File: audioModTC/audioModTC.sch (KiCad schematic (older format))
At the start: 41 parts, among them J1 Screw_Terminal_01x02, J2 703W-00/52, Q1 IRFP360LCPBF, Q2 IRFP360LCPBF, U1 NCP1117-12V, U2 74HC14, U3 NCP1117-5V, U4 UCC37321P, U5 UCC37322P

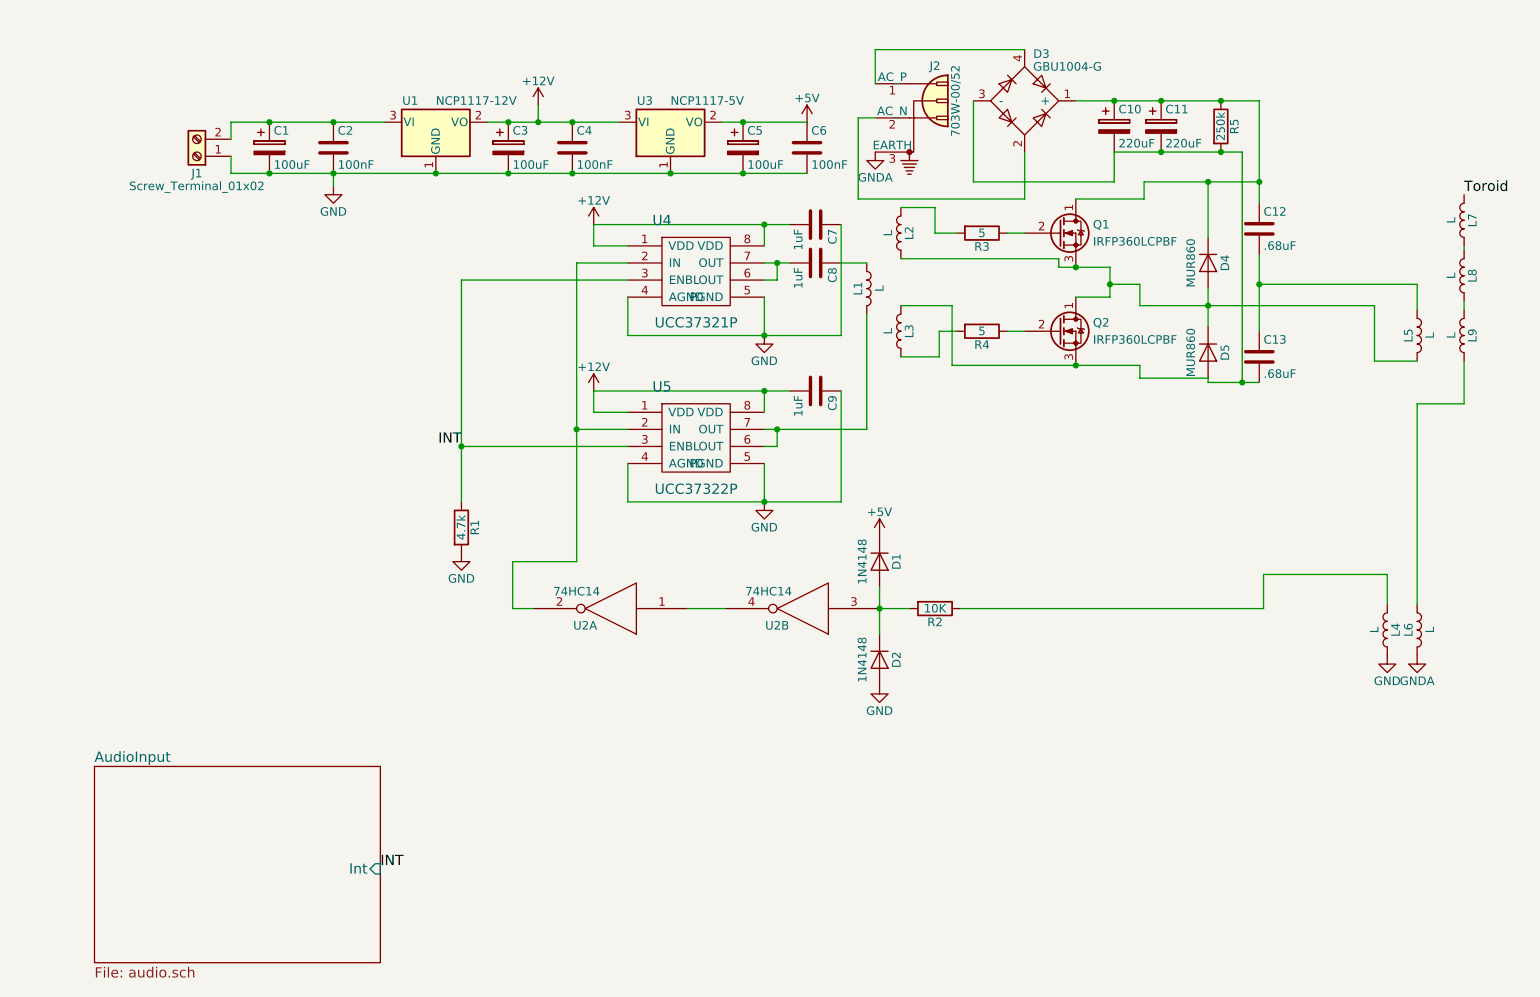
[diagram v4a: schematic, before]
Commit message: Finished footprints
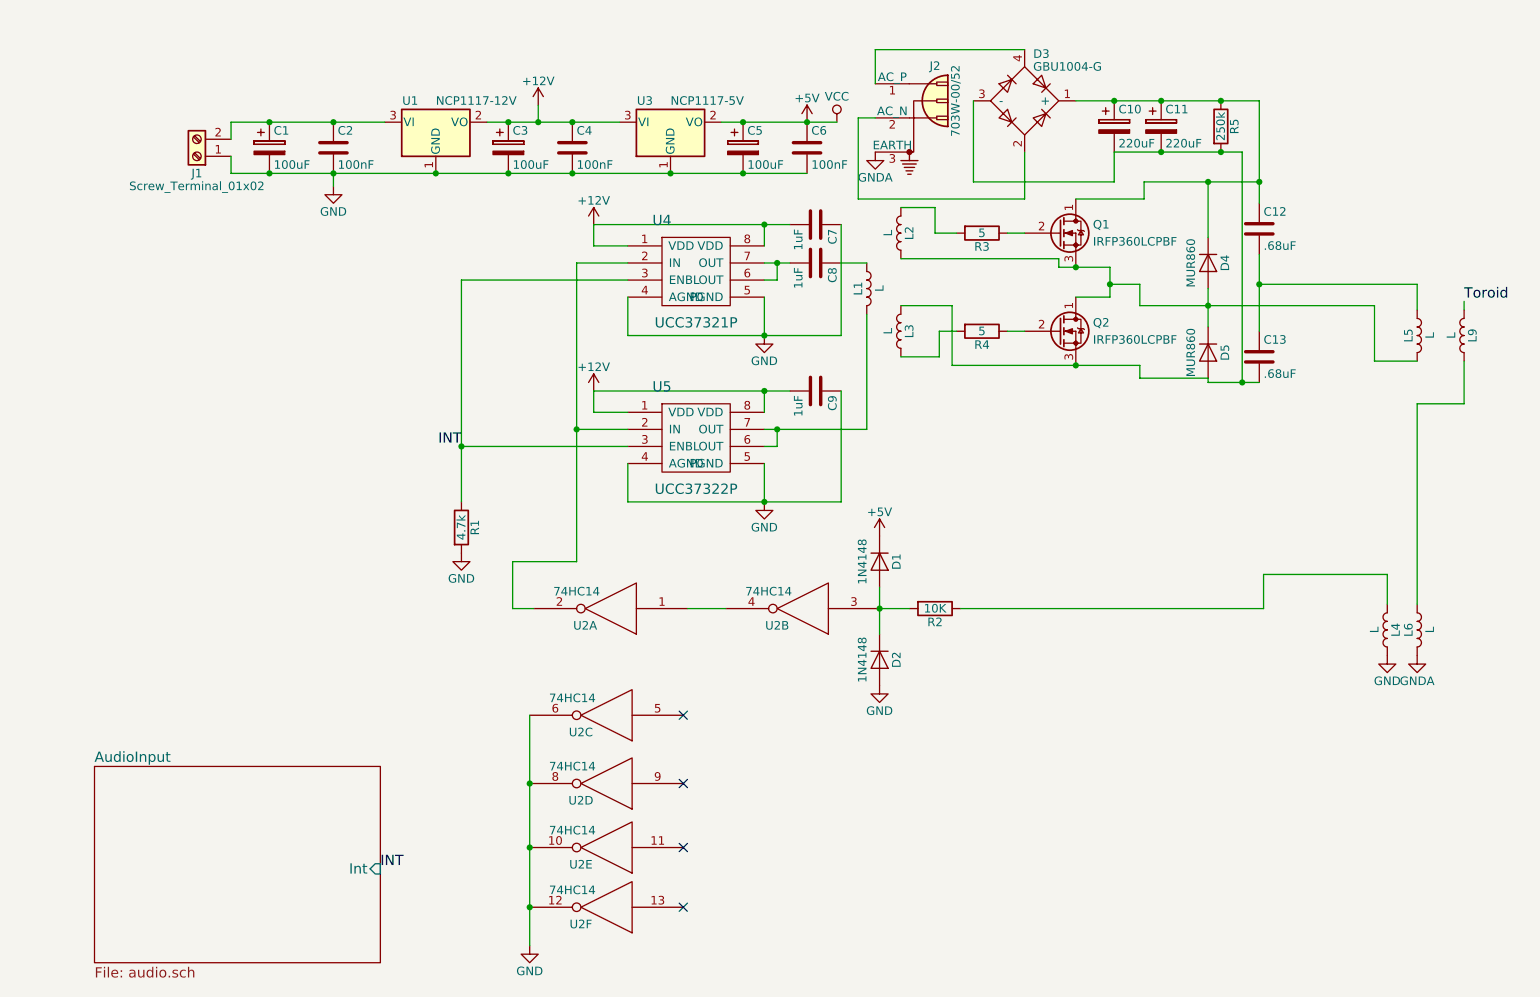
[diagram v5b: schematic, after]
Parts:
- removed L7, L8: L, symbol L
- added unit 3 of U2
- added unit 4 of U2
- added unit 5 of U2
- added unit 6 of U2
- L1, L2, L3, L4, L5, L6, L9: footprint (none) -> Inductors_THT:L_Radial_D7.0mm_P3.00mm
- U2: footprint (none) -> Housings_DIP:DIP-14_W7.62mm
- U4, U5: footprint (none) -> Housings_DIP:DIP-8_W7.62mm
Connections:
- net VCC is gone; now on net +5V: U2.14 (VCC), U2.14 (VCC)
- net +5V: now also U2.14 (VCC), U2.14 (VCC), U2.14 (VCC), U2.14 (VCC)
- net GND: now also U2.10, U2.12, U2.6, U2.7 (GND), U2.7 (GND), U2.7 (GND), U2.7 (GND), U2.8
- net Toroid: now also L9.2
- no-connect marks 0 -> 4
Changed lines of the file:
@@
 Connection ~ 3875 1625
 Wire Wire Line
-	5125 1325 5625 1325
+	5125 1325 5800 1325
 Connection ~ 5250 1325
 Connection ~ 4825 1625
@@
 F 0 "L5" V 9150 2575 50  0000 C CNN
 F 1 "L" V 9275 2575 50  0000 C CNN
-F 2 "" H 9200 2575 50  0001 C CNN
+F 2 "Inductors_THT:L_Radial_D7.0mm_P3.00mm" H 9200 2575 50  0001 C CNN
 F 3 "" H 9200 2575 50  0001 C CNN
 	1    9200 2575
@@
 F 0 "L3" V 6125 2550 50  0000 C CNN
 F 1 "L" V 6250 2550 50  0000 C CNN
-F 2 "" H 6175 2550 50  0001 C CNN
+F 2 "Inductors_THT:L_Radial_D7.0mm_P3.00mm" H 6175 2550 50  0001 C CNN
 F 3 "" H 6175 2550 50  0001 C CNN
 	1    6175 2550
@@
 F 0 "L2" V 6125 1975 50  0000 C CNN
 F 1 "L" V 6250 1975 50  0000 C CNN
-F 2 "" H 6175 1975 50  0001 C CNN
+F 2 "Inductors_THT:L_Radial_D7.0mm_P3.00mm" H 6175 1975 50  0001 C CNN
 F 3 "" H 6175 1975 50  0001 C CNN
 	1    6175 1975
@@
 F 0 "L1" V 5925 2300 50  0000 C CNN
 F 1 "L" V 6050 2300 50  0000 C CNN
-F 2 "" H 5975 2300 50  0001 C CNN
+F 2 "Inductors_THT:L_Radial_D7.0mm_P3.00mm" H 5975 2300 50  0001 C CNN
 F 3 "" H 5975 2300 50  0001 C CNN
 	1    5975 2300
@@
 F 0 "U4" H 4775 2500 60  0000 C CNN
 F 1 "UCC37321P" H 4975 1900 60  0000 C CNN
-F 2 "" H 4925 2200 60  0001 C CNN
+F 2 "Housings_DIP:DIP-8_W7.62mm" H 4925 2200 60  0001 C CNN
 F 3 "" H 4925 2200 60  0001 C CNN
 	1    4975 2200
@@
 F 0 "U5" H 4775 3475 60  0000 C CNN
 F 1 "UCC37322P" H 4975 2875 60  0000 C CNN
-F 2 "" H 4925 3175 60  0001 C CNN
+F 2 "Housings_DIP:DIP-8_W7.62mm" H 4925 3175 60  0001 C CNN
 F 3 "" H 4925 3175 60  0001 C CNN
 	1    4975 3175
@@
 F 0 "U2" H 4625 4275 50  0000 C CNN
 F 1 "74HC14" H 4675 4075 50  0000 C CNN
-F 2 "" H 4475 4175 50  0001 C CNN
+F 2 "Housings_DIP:DIP-14_W7.62mm" H 4475 4175 50  0001 C CNN
 F 3 "" H 4475 4175 50  0001 C CNN
 	1    4475 4175
@@
 F 0 "U2" H 5750 4275 50  0000 C CNN
 F 1 "74HC14" H 5800 4075 50  0000 C CNN
-F 2 "" H 5600 4175 50  0001 C CNN
+F 2 "Housings_DIP:DIP-14_W7.62mm" H 5600 4175 50  0001 C CNN
 F 3 "" H 5600 4175 50  0001 C CNN
 	2    5600 4175
@@
 F 0 "L6" V 9150 4300 50  0000 C CNN
 F 1 "L" V 9275 4300 50  0000 C CNN
-F 2 "" H 9200 4300 50  0001 C CNN
+F 2 "Inductors_THT:L_Radial_D7.0mm_P3.00mm" H 9200 4300 50  0001 C CNN
 F 3 "" H 9200 4300 50  0001 C CNN
 	1    9200 4300
@@
 F 0 "L4" V 8975 4300 50  0000 C CNN
 F 1 "L" V 9100 4300 50  0000 C CNN
-F 2 "" H 9025 4300 50  0001 C CNN
+F 2 "Inductors_THT:L_Radial_D7.0mm_P3.00mm" H 9025 4300 50  0001 C CNN
 F 3 "" H 9025 4300 50  0001 C CNN
 	1    9025 4300
@@
 F 0 "L9" V 9425 2575 50  0000 C CNN
 F 1 "L" V 9550 2575 50  0000 C CNN
-F 2 "" H 9475 2575 50  0001 C CNN
+F 2 "Inductors_THT:L_Radial_D7.0mm_P3.00mm" H 9475 2575 50  0001 C CNN
 F 3 "" H 9475 2575 50  0001 C CNN
 	1    9475 2575
 	-1   0    0    1
 $EndComp
-$Comp
-L L L8
-U 1 1 5A4AC75A
-P 9475 2225
-F 0 "L8" V 9425 2225 50  0000 C CNN
-F 1 "L" V 9550 2225 50  0000 C CNN
-F 2 "" H 9475 2225 50  0001 C CNN
-F 3 "" H 9475 2225 50  0001 C CNN
-	1    9475 2225
-	-1   0    0    1
-$EndComp
-$Comp
-L L L7
-U 1 1 5A4AC7D1
-P 9475 1900
-F 0 "L7" V 9425 1900 50  0000 C CNN
-F 1 "L" V 9550 1900 50  0000 C CNN
-F 2 "" H 9475 1900 50  0001 C CNN
-F 3 "" H 9475 1900 50  0001 C CNN
-	1    9475 1900
-	-1   0    0    1
-$EndComp
 Wire Wire Line
 	9200 4150 9200 2975
@@
 	9475 2975 9475 2725
 Wire Wire Line
-	9475 2050 9475 2075
-Wire Wire Line
 	9475 2375 9475 2425
-Text Label 9475 1750 0    60   ~ 0
+Text Label 9475 2375 0    60   ~ 0
 Toroid
 $Sheet
@@
 Wire Wire Line
 	5925 1300 6025 1300
+$Comp
+L 74HC14 U2
+U 3 1 5A4E733A
+P 4450 4800
+F 0 "U2" H 4600 4900 50  0000 C CNN
+F 1 "74HC14" H 4650 4700 50  0000 C CNN
+F 2 "Housings_DIP:DIP-14_W7.62mm" H 4450 4800 50  0001 C CNN
+F 3 "" H 4450 4800 50  0001 C CNN
+	3    4450 4800
+	-1   0    0    1
+$EndComp
+$Comp
+L 74HC14 U2
+U 4 1 5A4E744D
+P 4450 5200
+F 0 "U2" H 4600 5300 50  0000 C CNN
+F 1 "74HC14" H 4650 5100 50  0000 C CNN
+F 2 "Housings_DIP:DIP-14_W7.62mm" H 4450 5200 50  0001 C CNN
+F 3 "" H 4450 5200 50  0001 C CNN
+	4    4450 5200
+	-1   0    0    1
+$EndComp
+$Comp
+L 74HC14 U2
+U 5 1 5A4E7818
+P 4450 5575
+F 0 "U2" H 4600 5675 50  0000 C CNN
+F 1 "74HC14" H 4650 5475 50  0000 C CNN
+F 2 "Housings_DIP:DIP-14_W7.62mm" H 4450 5575 50  0001 C CNN
+F 3 "" H 4450 5575 50  0001 C CNN
+	5    4450 5575
+	-1   0    0    1
+$EndComp
+$Comp
+L 74HC14 U2
+U 6 1 5A4E7919
+P 4450 5925
+F 0 "U2" H 4600 6025 50  0000 C CNN
+F 1 "74HC14" H 4650 5825 50  0000 C CNN
+F 2 "Housings_DIP:DIP-14_W7.62mm" H 4450 5925 50  0001 C CNN
+F 3 "" H 4450 5925 50  0001 C CNN
+	6    4450 5925
+	-1   0    0    1
+$EndComp
+NoConn ~ 4900 4800
+NoConn ~ 4900 5200
+NoConn ~ 4900 5575
+NoConn ~ 4900 5925
+$Comp
+L GND #PWR014
+U 1 1 5A4E85FF
+P 4000 6150
+F 0 "#PWR014" H 4000 5900 50  0001 C CNN
+F 1 "GND" H 4000 6000 50  0000 C CNN
+F 2 "" H 4000 6150 50  0001 C CNN
+F 3 "" H 4000 6150 50  0001 C CNN
+	1    4000 6150
+	1    0    0    -1
+$EndComp
+Wire Wire Line
+	4000 4800 4000 6150
+Connection ~ 4000 5200
+Connection ~ 4000 5575
+Connection ~ 4000 5925
+$Comp
+L VCC #PWR015
+U 1 1 5A4F18EE
+P 5800 1325
+F 0 "#PWR015" H 5800 1175 50  0001 C CNN
+F 1 "VCC" H 5800 1475 50  0000 C CNN
+F 2 "" H 5800 1325 50  0001 C CNN
+F 3 "" H 5800 1325 50  0001 C CNN
+	1    5800 1325
+	1    0    0    -1
+$EndComp
+Connection ~ 5625 1325
 $EndSCHEMATC

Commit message: Finished footprints fo real
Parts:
- removed L1, L2, L3, L4, L6: L, Inductors_THT:L_Radial_D7.0mm_P3.00mm, symbol L
- added T1: Transformer_1P_2S, Custom:Trifilar-Transformer-1P-2S, symbol Transformer_1P_2S
- added T2: Transformer_1P_1S, Custom:RM-4-Transformer, symbol Transformer_1P_1S
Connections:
- net GND: now also T2.2 (AB)
- net GNDA: now also T2.3 (SA)
- net at C10.2, C11.2, C13.2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: now also T1.5 (SC)
- net at D4.2 (A), D5.1 (K), L5.2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: now also T1.4 (SB)
- net at Q2.2 (G): now also R4.2; no longer R4.1
- net at R3.2: now also T1.3 (SA)
- net at C8.1: now also T1.1 (AA)
- net at U5.6 (OUT), U5.7 (OUT): now also T1.2 (AB)
- net at R2.1: now also T2.1 (AA)
- net at L9.1: now also T2.4 (SB)
- new net: R4.1, T1.6 (SD)
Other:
- moved on the sheet: R3, R4
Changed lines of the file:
@@
 Wire Wire Line
 	7575 2825 7575 2750
-Wire Wire Line
-	7575 2750 6475 2750
 $Comp
 L L L5
@@
 Connection ~ 7975 2400
 Wire Wire Line
-	7100 2175 7400 2175
-Wire Wire Line
 	7400 2175 7400 2350
 Wire Wire Line
@@
 L R R3
 U 1 1 5A4A8F43
-P 6650 1975
-F 0 "R3" V 6730 1975 50  0000 C CNN
-F 1 "5" V 6650 1975 50  0000 C CNN
-F 2 "Resistors_SMD:R_0603" V 6580 1975 50  0001 C CNN
-F 3 "" H 6650 1975 50  0001 C CNN
-	1    6650 1975
+P 6750 2075
+F 0 "R3" V 6830 2075 50  0000 C CNN
+F 1 "5" V 6750 2075 50  0000 C CNN
+F 2 "Resistors_SMD:R_0603" V 6680 2075 50  0001 C CNN
+F 3 "" H 6750 2075 50  0001 C CNN
+	1    6750 2075
 	0    1    1    0
 $EndComp
@@
 L R R4
 U 1 1 5A4A8FB6
-P 6650 2550
-F 0 "R4" V 6730 2550 50  0000 C CNN
-F 1 "5" V 6650 2550 50  0000 C CNN
-F 2 "Resistors_SMD:R_0603" V 6580 2550 50  0001 C CNN
-F 3 "" H 6650 2550 50  0001 C CNN
-	1    6650 2550
-	0    1    1    0
-$EndComp
-Wire Wire Line
-	6900 2550 6800 2550
-Wire Wire Line
-	6900 1975 6800 1975
-$Comp
-L L L3
-U 1 1 5A4A91A3
-P 6175 2550
-F 0 "L3" V 6125 2550 50  0000 C CNN
-F 1 "L" V 6250 2550 50  0000 C CNN
-F 2 "Inductors_THT:L_Radial_D7.0mm_P3.00mm" H 6175 2550 50  0001 C CNN
-F 3 "" H 6175 2550 50  0001 C CNN
-	1    6175 2550
-	-1   0    0    1
-$EndComp
-$Comp
-L L L2
-U 1 1 5A4A9244
-P 6175 1975
-F 0 "L2" V 6125 1975 50  0000 C CNN
-F 1 "L" V 6250 1975 50  0000 C CNN
-F 2 "Inductors_THT:L_Radial_D7.0mm_P3.00mm" H 6175 1975 50  0001 C CNN
-F 3 "" H 6175 1975 50  0001 C CNN
-	1    6175 1975
-	-1   0    0    1
-$EndComp
-Wire Wire Line
-	6175 2400 6475 2400
-Wire Wire Line
-	6475 2400 6475 2750
+P 6900 2700
+F 0 "R4" V 6980 2700 50  0000 C CNN
+F 1 "5" V 6900 2700 50  0000 C CNN
+F 2 "Resistors_SMD:R_0603" V 6830 2700 50  0001 C CNN
+F 3 "" H 6900 2700 50  0001 C CNN
+	1    6900 2700
+	-1   0    0    1
+$EndComp
 Connection ~ 7200 2750
-Wire Wire Line
-	6175 2700 6400 2700
-Wire Wire Line
-	6400 2700 6400 2550
-Wire Wire Line
-	6400 2550 6500 2550
-Wire Wire Line
-	6500 1975 6375 1975
-Wire Wire Line
-	6375 1975 6375 1825
-Wire Wire Line
-	6375 1825 6175 1825
-Wire Wire Line
-	6175 2125 7100 2125
-Wire Wire Line
-	7100 2125 7100 2175
 Connection ~ 7200 2175
-$Comp
-L L L1
-U 1 1 5A4A9AF1
-P 5975 2300
-F 0 "L1" V 5925 2300 50  0000 C CNN
-F 1 "L" V 6050 2300 50  0000 C CNN
-F 2 "Inductors_THT:L_Radial_D7.0mm_P3.00mm" H 5975 2300 50  0001 C CNN
-F 3 "" H 5975 2300 50  0001 C CNN
-	1    5975 2300
-	1    0    0    -1
-$EndComp
 $Comp
 L C C8
@@
 	5375 3125 5975 3125
 Wire Wire Line
-	5975 3125 5975 2450
-Wire Wire Line
 	5450 3225 5450 3125
 Connection ~ 5450 3125
@@
 $EndComp
 $Comp
-L L L6
-U 1 1 5A4AC021
-P 9200 4300
-F 0 "L6" V 9150 4300 50  0000 C CNN
-F 1 "L" V 9275 4300 50  0000 C CNN
-F 2 "Inductors_THT:L_Radial_D7.0mm_P3.00mm" H 9200 4300 50  0001 C CNN
-F 3 "" H 9200 4300 50  0001 C CNN
-	1    9200 4300
-	1    0    0    -1
-$EndComp
-$Comp
-L L L4
-U 1 1 5A4AC22E
-P 9025 4300
-F 0 "L4" V 8975 4300 50  0000 C CNN
-F 1 "L" V 9100 4300 50  0000 C CNN
-F 2 "Inductors_THT:L_Radial_D7.0mm_P3.00mm" H 9025 4300 50  0001 C CNN
-F 3 "" H 9025 4300 50  0001 C CNN
-	1    9025 4300
-	-1   0    0    1
-$EndComp
-$Comp
 L GND #PWR012
 U 1 1 5A4AC39F
-P 9025 4450
-F 0 "#PWR012" H 9025 4200 50  0001 C CNN
-F 1 "GND" H 9025 4300 50  0000 C CNN
-F 2 "" H 9025 4450 50  0001 C CNN
-F 3 "" H 9025 4450 50  0001 C CNN
-	1    9025 4450
+P 8350 4325
+F 0 "#PWR012" H 8350 4075 50  0001 C CNN
+F 1 "GND" H 8350 4175 50  0000 C CNN
+F 2 "" H 8350 4325 50  0001 C CNN
+F 3 "" H 8350 4325 50  0001 C CNN
+	1    8350 4325
 	1    0    0    -1
 $EndComp
@@
 L GNDA #PWR013
 U 1 1 5A4AC49B
-P 9200 4450
-F 0 "#PWR013" H 9200 4200 50  0001 C CNN
-F 1 "GNDA" H 9200 4300 50  0000 C CNN
-F 2 "" H 9200 4450 50  0001 C CNN
-F 3 "" H 9200 4450 50  0001 C CNN
-	1    9200 4450
+P 9150 4325
+F 0 "#PWR013" H 9150 4075 50  0001 C CNN
+F 1 "GNDA" H 9150 4175 50  0000 C CNN
+F 2 "" H 9150 4325 50  0001 C CNN
+F 3 "" H 9150 4325 50  0001 C CNN
+	1    9150 4325
 	1    0    0    -1
 $EndComp
 Wire Wire Line
 	6525 4175 8300 4175
-Wire Wire Line
-	8300 4175 8300 3975
-Wire Wire Line
-	8300 3975 9025 3975
-Wire Wire Line
-	9025 3975 9025 4150
 $Comp
 L L L9
@@
 $EndComp
 Wire Wire Line
-	9200 4150 9200 2975
-Wire Wire Line
-	9200 2975 9475 2975
+	9150 2975 9475 2975
 Wire Wire Line
 	9475 2975 9475 2725
@@
 $EndComp
 Connection ~ 5625 1325
+$Comp
+L Transformer_1P_1S T2
+U 1 1 5A5138E6
+P 8750 4125
+F 0 "T2" H 8750 4375 50  0000 C CNN
+F 1 "Transformer_1P_1S" H 8750 3825 50  0000 C CNN
+F 2 "Custom:RM-4-Transformer" H 8750 4125 50  0001 C CNN
+F 3 "" H 8750 4125 50  0001 C CNN
+	1    8750 4125
+	1    0    0    -1
+$EndComp
+Wire Wire Line
+	8300 4175 8300 3925
+Wire Wire Line
+	8300 3925 8350 3925
+Wire Wire Line
+	9150 3925 9150 2975
+$Comp
+L Transformer_1P_2S T1
+U 1 1 5A514F7B
+P 6375 2350
+F 0 "T1" H 6375 2850 50  0000 C CNN
+F 1 "Transformer_1P_2S" H 6375 1850 50  0000 C CNN
+F 2 "Custom:Trifilar-Transformer-1P-2S" H 6375 2350 50  0001 C CNN
+F 3 "" H 6375 2350 50  0001 C CNN
+	1    6375 2350
+	1    0    0    -1
+$EndComp
+Wire Wire Line
+	5975 3125 5975 2550
+Wire Wire Line
+	6900 2850 6775 2850
+Wire Wire Line
+	6775 2850 6775 2750
+Wire Wire Line
+	7575 2750 7200 2750
+Wire Wire Line
+	7200 2750 7200 2975
+Wire Wire Line
+	7200 2975 6700 2975
+Wire Wire Line
+	6700 2975 6700 2550
+Wire Wire Line
+	6700 2550 6775 2550
+Wire Wire Line
+	6775 2550 6775 2450
+Wire Wire Line
+	6900 1975 6900 2075
+Wire Wire Line
+	6600 2075 6600 2000
+Wire Wire Line
+	6600 2000 6775 2000
+Wire Wire Line
+	6775 2000 6775 1950
+Wire Wire Line
+	6925 2175 7400 2175
+Wire Wire Line
+	6925 2175 6925 2250
+Wire Wire Line
+	6925 2250 6775 2250
 $EndSCHEMATC

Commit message: Finished PCB
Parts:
- C10, C11: footprint Capacitors_THT:CP_Radial_D6.3mm_P2.50mm -> Capacitors_THT:CP_Radial_D25.0mm_P10.00mm_SnapIn
- C12, C13: footprint Capacitors_SMD:C_0603 -> Capacitors_THT:C_Rect_L26.5mm_W7.0mm_P22.50mm_MKS4
- C2, C4, C6: value 100nF -> .1uF
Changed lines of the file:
@@
 P 2850 1475
 F 0 "C2" H 2875 1575 50  0000 L CNN
-F 1 "100nF" H 2875 1375 50  0000 L CNN
+F 1 ".1uF" H 2875 1375 50  0000 L CNN
 F 2 "Capacitors_SMD:C_0603" H 2888 1325 50  0001 C CNN
 F 3 "" H 2850 1475 50  0001 C CNN
@@
 P 4250 1475
 F 0 "C4" H 4275 1575 50  0000 L CNN
-F 1 "100nF" H 4275 1375 50  0000 L CNN
+F 1 ".1uF" H 4275 1375 50  0000 L CNN
 F 2 "Capacitors_SMD:C_0603" H 4288 1325 50  0001 C CNN
 F 3 "" H 4250 1475 50  0001 C CNN
@@
 P 5625 1475
 F 0 "C6" H 5650 1575 50  0000 L CNN
-F 1 "100nF" H 5650 1375 50  0000 L CNN
+F 1 ".1uF" H 5650 1375 50  0000 L CNN
 F 2 "Capacitors_SMD:C_0603" H 5663 1325 50  0001 C CNN
 F 3 "" H 5625 1475 50  0001 C CNN
@@
 F 0 "C10" H 7450 1450 50  0000 L CNN
 F 1 "220uF" H 7450 1250 50  0000 L CNN
-F 2 "Capacitors_THT:CP_Radial_D6.3mm_P2.50mm" H 7463 1200 50  0001 C CNN
+F 2 "Capacitors_THT:CP_Radial_D25.0mm_P10.00mm_SnapIn" H 7463 1200 50  0001 C CNN
 F 3 "" H 7425 1350 50  0001 C CNN
 	1    7425 1350
@@
 F 0 "C11" H 7725 1450 50  0000 L CNN
 F 1 "220uF" H 7725 1250 50  0000 L CNN
-F 2 "Capacitors_THT:CP_Radial_D6.3mm_P2.50mm" H 7738 1200 50  0001 C CNN
+F 2 "Capacitors_THT:CP_Radial_D25.0mm_P10.00mm_SnapIn" H 7738 1200 50  0001 C CNN
 F 3 "" H 7700 1350 50  0001 C CNN
 	1    7700 1350
@@
 F 0 "C12" H 8300 2050 50  0000 L CNN
 F 1 ".68uF" H 8300 1850 50  0000 L CNN
-F 2 "Capacitors_SMD:C_0603" H 8313 1800 50  0001 C CNN
+F 2 "Capacitors_THT:C_Rect_L26.5mm_W7.0mm_P22.50mm_MKS4" H 8313 1800 50  0001 C CNN
 F 3 "" H 8275 1950 50  0001 C CNN
 	1    8275 1950
@@
 F 0 "C13" H 8300 2800 50  0000 L CNN
 F 1 ".68uF" H 8300 2600 50  0000 L CNN
-F 2 "Capacitors_SMD:C_0603" H 8313 2550 50  0001 C CNN
+F 2 "Capacitors_THT:C_Rect_L26.5mm_W7.0mm_P22.50mm_MKS4" H 8313 2550 50  0001 C CNN
 F 3 "" H 8275 2700 50  0001 C CNN
 	1    8275 2700
